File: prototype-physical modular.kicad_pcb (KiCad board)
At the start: 2 copper layers, 100 x 164 mm, 183 parts, among them CON1 BARREL_JACK, CON2 SD_Card_SEEEDOPL, IC1 ATMEGA2560-A, P1 POWER, P10 PC, P11 CONN_UART, P12 PJ, P15 PH, P16 PF, P18 3VI2C, P19 PIGPIO, P20 MIDI_IN, P21 MIDI_OUT, P22 BUSTI, P23 BUSTO, P3 SPI, P7 PA, Q1 BSS138, Q2 BSS138, Q3 BSS138, Q4 BSS138, Q5 BSS138, Q6 BSS138, SW1 SW_PUSH, SW10 SW_PUSH, SW11 SW_PUSH, SW12 SW_PUSH, SW13 SW_PUSH, SW14 SW_PUSH, SW2 ROTARY_ENCODER_SWITCH, SW3 SW_PUSH, SW4 SW_PUSH, SW5 SW_PUSH, SW6 SW_PUSH, SW7 SW_PUSH, SW8 SW_PUSH, SW9 SW_PUSH, U1 NCP1117ST50T3G, U2 6N138, Y1 16MHz

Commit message: routed
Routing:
- net GND: track 0.00 -> 1129.8 mm, vias 0 -> 27
- net +5V: track 0.00 -> 814.1 mm, vias 0 -> 51
- net /MUXAX0: track 0.00 -> 257.5 mm, vias 0 -> 6
- net /BUS_COM: track 0.00 -> 250.1 mm, vias 0 -> 5
- net /TX3: track 0.00 -> 241.9 mm, vias 0 -> 6
- net /MUXAX1: track 0.00 -> 228.1 mm, vias 0 -> 6
- net /MUXAX3: track 0.00 -> 215.5 mm, vias 0 -> 3
- net /MUXAX2: track 0.00 -> 204.7 mm, vias 0 -> 4
- net Net-(IC1-Pad65): track 0.00 -> 191.4 mm, vias 0 -> 2
- net /MUXBX6: track 0.00 -> 178.5 mm, vias 0 -> 4
- net /MUXBX5: track 0.00 -> 175.0 mm, vias 0 -> 2
- net /MUXAX4: track 0.00 -> 163.0 mm, vias 0 -> 3
- net /MUXBX4: track 0.00 -> 161.9 mm, vias 0 -> 4
- net /MUXBX0: track 0.00 -> 144.8 mm, vias 0 -> 5
- net Net-(IC1-Pad1): track 0.00 -> 144.5 mm, vias 0 -> 2
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
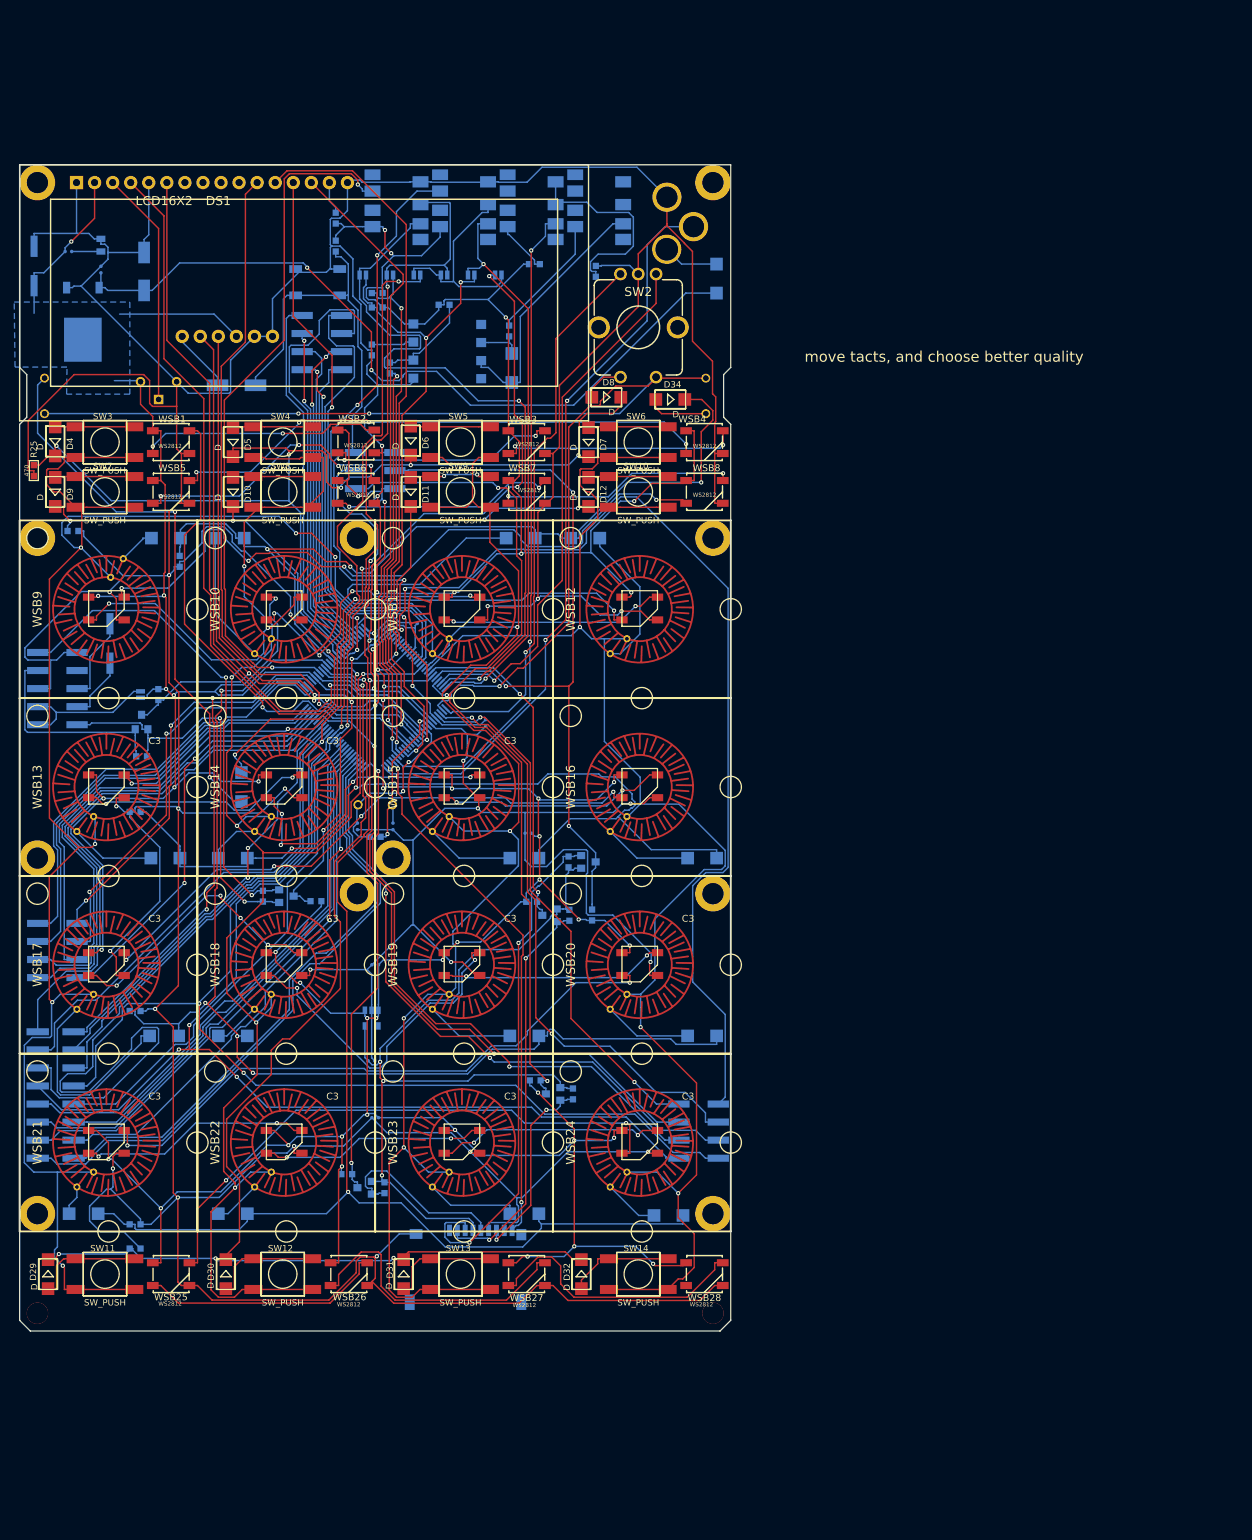
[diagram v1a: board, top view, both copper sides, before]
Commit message: moved a couple of components around, updating the routing
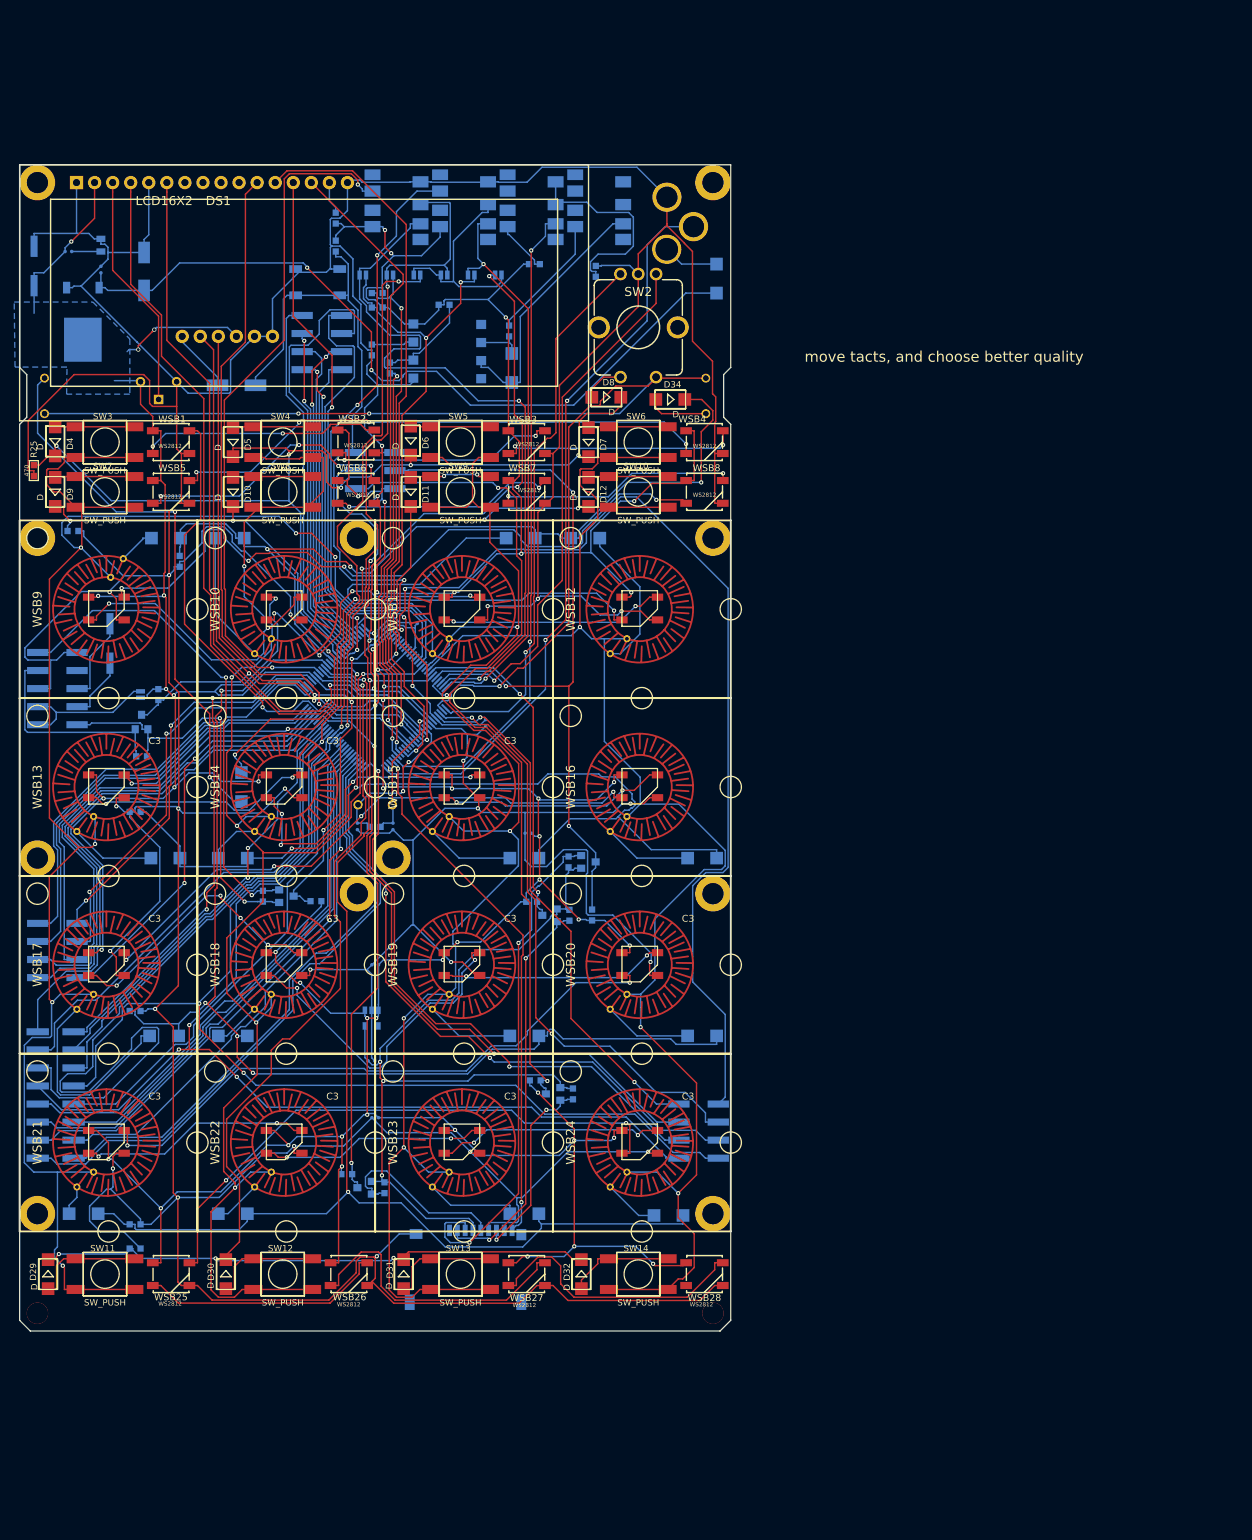
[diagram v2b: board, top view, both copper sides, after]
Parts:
- moved R8 1.40 mm to (50.0, 93.1)
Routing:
- net Net-(C8-Pad1): track 23.1 -> 19.5 mm, vias 2 -> 1
- net Net-(C9-Pad1): track 24.9 -> 22.9 mm
- net +5V: track 814.1 -> 814.0 mm, vias 51 -> 53

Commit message: optimize design rules, location of some components, added labels to every connector pin
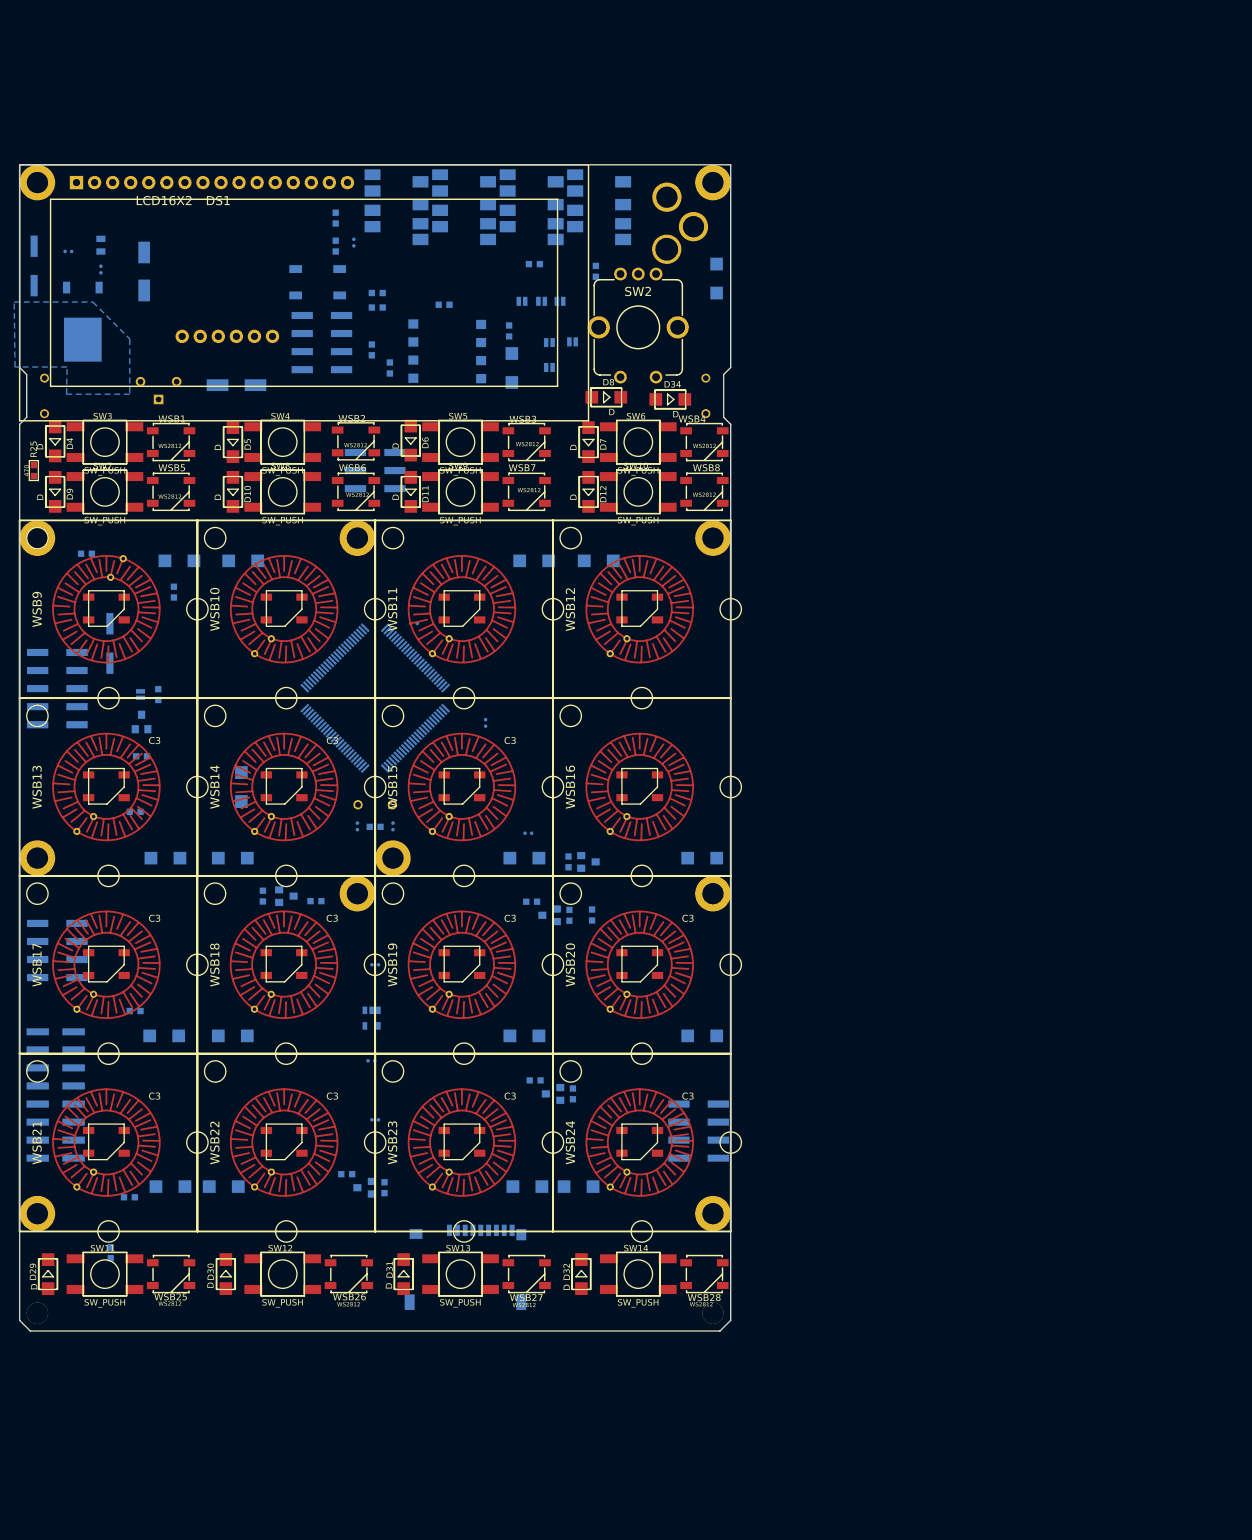
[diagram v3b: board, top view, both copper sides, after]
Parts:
- moved C4 36.7 mm to (47.0, 10.9), turned to 180 degrees
- moved JP3 24.2 mm to (76.0, 19.2)
- moved JP4 22.7 mm to (70.7, 19.2)
- moved PJ2COM1 20.9 mm to (74.5, 25.0)
- moved JP1 20.4 mm to (77.8, 24.9)
- moved PJ1COM1 14.9 mm to (74.5, 28.5), turned to 0 degrees
- moved D28 13.3 mm to (78.6, 143.7)
- moved D25 12.8 mm to (21.2, 143.7)
- moved JP5 10.6 mm to (73.4, 19.2)
- moved R27 4.41 mm to (21.7, 60.1)
- moved D26 4.01 mm to (28.7, 143.7)
- moved R30 3.88 mm to (15.4, 145.2)
- moved D27 3.82 mm to (71.4, 143.7)
- moved D16 3.72 mm to (81.4, 55.7)
- moved R26 3.72 mm to (9.40, 54.7)
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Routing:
- net GND: track 1130.2 -> 0.00 mm, vias 27 -> 0
- net +5V: track 814.0 -> 0.00 mm, vias 53 -> 0
- net /MUXAX0: track 257.5 -> 0.00 mm, vias 6 -> 0
- net /BUS_COM: track 250.1 -> 0.00 mm, vias 5 -> 0
- net /TX3: track 241.9 -> 0.00 mm, vias 6 -> 0
- net /MUXAX1: track 228.1 -> 0.00 mm, vias 6 -> 0
- net /MUXAX3: track 215.5 -> 0.00 mm, vias 3 -> 0
- net /MUXAX2: track 204.7 -> 0.00 mm, vias 4 -> 0
- net Net-(IC1-Pad65): track 191.4 -> 0.00 mm, vias 2 -> 0
- net /MUXBX6: track 178.5 -> 0.00 mm, vias 4 -> 0
- net /MUXBX5: track 175.0 -> 0.00 mm, vias 2 -> 0
- net /MUXAX4: track 163.0 -> 0.00 mm, vias 3 -> 0
- net /MUXBX4: track 161.9 -> 0.00 mm, vias 4 -> 0
- net /MUXBX0: track 144.8 -> 0.00 mm, vias 5 -> 0
- net Net-(IC1-Pad1): track 144.5 -> 0.00 mm, vias 2 -> 0
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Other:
- net class Default: clearance 0.2032 -> 0.127; trace_width 0.2032 -> 0.1524
- net class power added: clearance 0.127, trace_width 0.2032, via_dia 0.6, via_drill 0.4
- rule trace_clearance: 0.2032 -> 0.127
- rule trace_min: 0.2 -> 0.1016
- board text added: "+5V"
- board text added: "3vRX"
- board text added: "3vTX"
- board text added: "5vCLK"
- board text added: "5vMISO"
- board text added: "5vMOSI"
- board text added: "5vRESET"
- board text added: "AUTOTEL.CO calculator 10.11.2017"
- board text added: "BUS_COM"
- board text added: "GND"
- board text added: "PA0"
- board text added: "PA1"
- board text added: "PA2"
- board text added: "PA3"
- board text added: "PA4"
- board text added: "PA5"
- board text added: "PA6"
- board text added: "PA7"
- board text added: "PC0"
- board text added: "PC1"
- board text added: "PC2"
- board text added: "PC3"
- board text added: "PC4"
- board text added: "PC5"
- board text added: "PC6"
- board text added: "PC7"
- board text added: "PF0"
- board text added: "PF1"
- board text added: "PF2"
- board text added: "PF3"
- board text added: "PF4"
- board text added: "PF5"
- board text added: "PF6"
- board text added: "PF7"
- board text added: "PG0"
- board text added: "PG1"
- board text added: "PG2"
- board text added: "PG3"
- board text added: "PG4"
- board text added: "PG5"
- board text added: "PI_3V3"
- board text added: "PI_5V"
- board text added: "PI_SCL"
- board text added: "PI_SDA"
- board text added: "PJ2"
- board text added: "PJ3"
- board text added: "PJ4"
- board text added: "PJ5"
- board text added: "PJ6"
- board text added: "PJ7"
- board text added: "TX3"
- board text removed: "AUTOTEL.CO calculator 20.10.2017"
- board text removed: "move tacts, and choose better quality"

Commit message: new go at routing
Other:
- net class Default: trace_width 0.1524 -> 0.2
- net class power: trace_width 0.2032 -> 0.3
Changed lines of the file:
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@@
     (38 B.Mask user)
     (39 F.Mask user)
-    (40 Dwgs.User user hide)
+    (40 Dwgs.User user)
     (41 Cmts.User user)
     (42 Eco1.User user)
@@
   )
   (setup
-    (last_trace_width 0.1524)
+    (last_trace_width 0.2)
     (trace_clearance 0.127)
     (zone_clearance 0.508)
@@
   (net_class Default "This is the default net class."
     (clearance 0.127)
-    (trace_width 0.1524)
+    (trace_width 0.2)
     (via_dia 0.6)
     (via_drill 0.4)
@@
   (net_class power ""
     (clearance 0.127)
-    (trace_width 0.2032)
+    (trace_width 0.3)
     (via_dia 0.6)
     (via_drill 0.4)
